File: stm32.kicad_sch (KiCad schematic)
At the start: 7 parts, among them J5 3220-10-0100-00, SW1 RotaryEncoder, U2 STM32G484CETx, U4 TVS0500DRV, Y1 32.768KHz

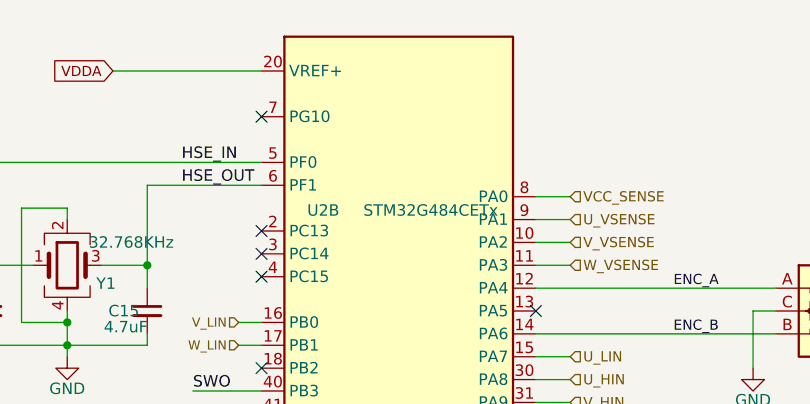
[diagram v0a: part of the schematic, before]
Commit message: Buck layout; MOSFET layout
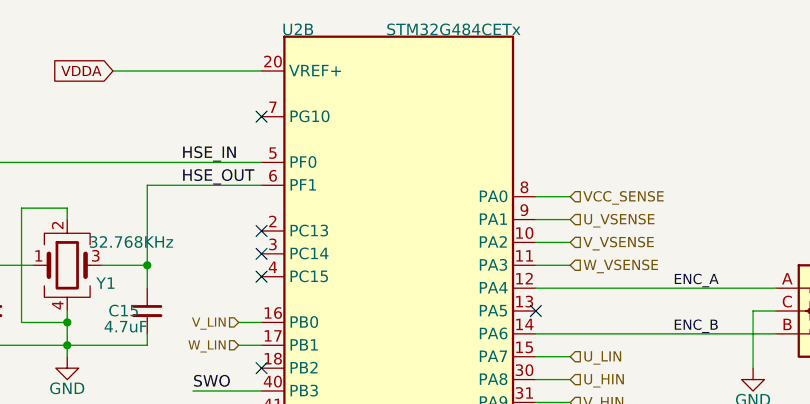
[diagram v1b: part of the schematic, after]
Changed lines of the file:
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@@
 		(on_board yes)
 		(dnp no)
-		(fields_autoplaced yes)
 		(property "Reference" "U2"
-			(at 169.418 67.564 0)
+			(at 166.624 47.498 0)
 			(effects
 				(font
@@
 		)
 		(property "Value" "STM32G484CETx"
-			(at 181.356 67.564 0)
+			(at 183.896 47.498 0)
 			(effects
 				(font

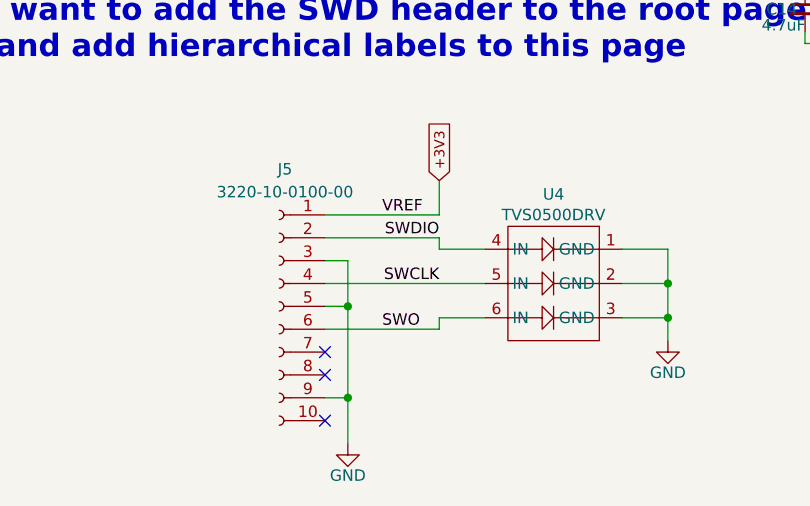
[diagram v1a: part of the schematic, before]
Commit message: PDN complete
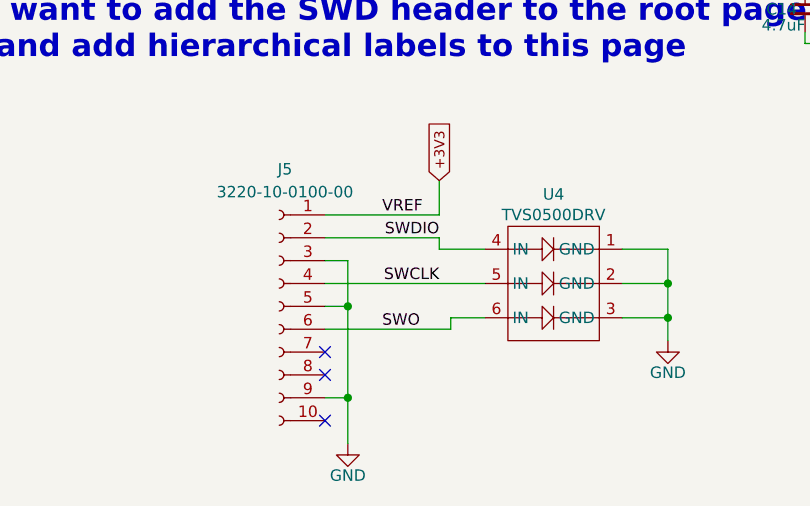
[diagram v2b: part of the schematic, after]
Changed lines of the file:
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@@
 	(wire
 		(pts
-			(xy 78.74 114.3) (xy 91.44 114.3)
+			(xy 78.74 114.3) (xy 92.71 114.3)
 		)
 		(stroke
@@
 	(wire
 		(pts
-			(xy 91.44 105.41) (xy 91.44 104.14)
+			(xy 91.44 104.14) (xy 91.44 105.41)
 		)
 		(stroke
@@
 	(wire
 		(pts
+			(xy 92.71 113.03) (xy 92.71 114.3)
+		)
+		(stroke
+			(width 0)
+			(type default)
+		)
+	)
+	(wire
+		(pts
 			(xy 140.97 82.55) (xy 140.97 83.82)
 		)
@@
 	(wire
 		(pts
-			(xy 91.44 113.03) (xy 91.44 114.3)
-		)
-		(stroke
-			(width 0)
-			(type default)
-		)
-	)
-	(wire
-		(pts
-			(xy 91.44 113.03) (xy 96.52 113.03)
-		)
-		(stroke
+			(xy 92.71 113.03) (xy 96.52 113.03)
+		)
+		(stroke

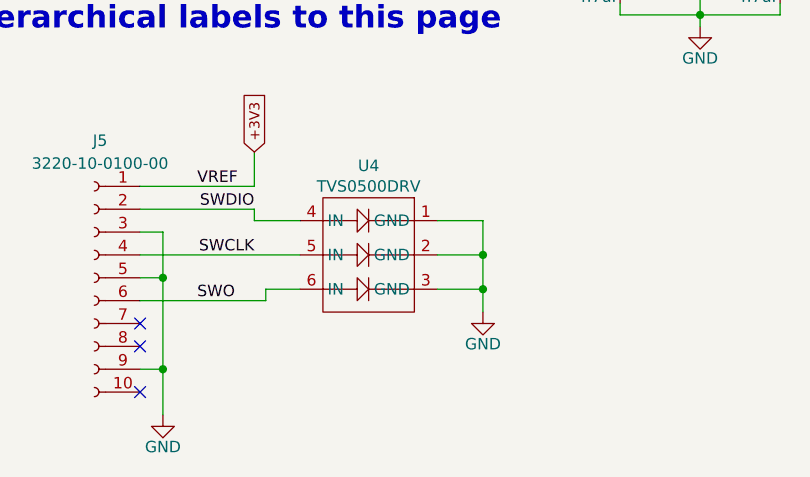
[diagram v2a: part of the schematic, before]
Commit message: improving MOSFET decap placements
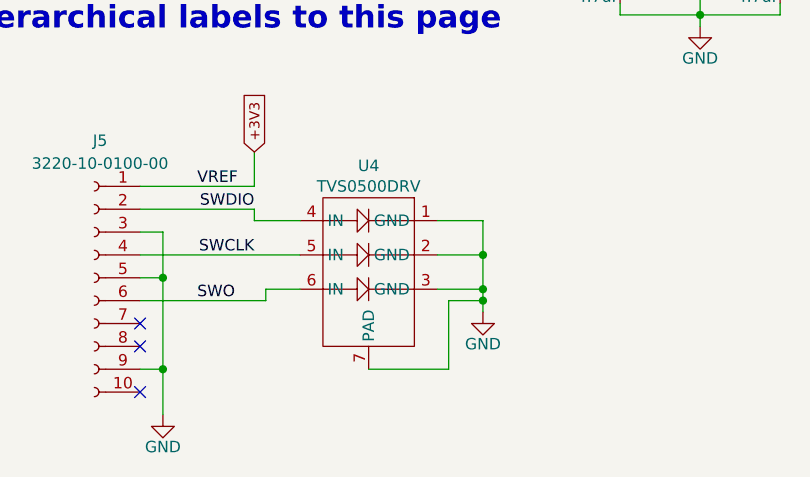
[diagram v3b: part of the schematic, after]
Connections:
- net GND: now also U4.7 (PAD)
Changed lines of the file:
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@@
+	)
+	(junction
+		(at 116.84 114.3)
+		(diameter 0)
+		(color 0 0 0 0)
 	)
 	(junction
@@
 	(wire
 		(pts
+			(xy 113.03 114.3) (xy 116.84 114.3)
+		)
+		(stroke
+			(width 0)
+			(type default)
+		)
+	)
+	(wire
+		(pts
 			(xy 162.56 62.23) (xy 132.08 62.23)
 		)
@@
 	(wire
 		(pts
+			(xy 104.14 121.92) (xy 113.03 121.92)
+		)
+		(stroke
+			(width 0)
+			(type default)
+		)
+	)
+	(wire
+		(pts
 			(xy 81.28 121.92) (xy 81.28 127)
 		)
@@
 	(wire
 		(pts
+			(xy 113.03 121.92) (xy 113.03 114.3)
+		)
+		(stroke
+			(width 0)
+			(type default)
+		)
+	)
+	(wire
+		(pts
 			(xy 91.44 101.6) (xy 78.74 101.6)
 		)
@@
 	(wire
 		(pts
-			(xy 116.84 113.03) (xy 116.84 115.57)
+			(xy 116.84 113.03) (xy 116.84 114.3)
 		)
 		(stroke
@@
 		(pts
 			(xy 193.04 71.12) (xy 196.85 71.12)
+		)
+		(stroke
+			(width 0)
+			(type default)
+		)
+	)
+	(wire
+		(pts
+			(xy 116.84 114.3) (xy 116.84 115.57)
 		)
 		(stroke
@@
 		(pin "4"
 		)
+		(pin "7"
+		)
 		(instances
